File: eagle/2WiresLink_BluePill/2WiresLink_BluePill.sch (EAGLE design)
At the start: 55 parts, among them IC1 TPS54060DGQ, IC3 SN74LVC1G240DBVR, IC6 TS3021ILT

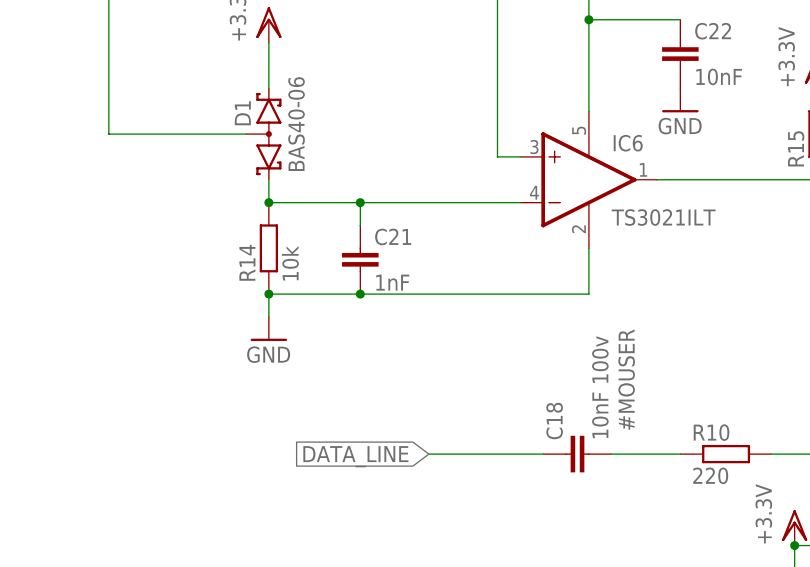
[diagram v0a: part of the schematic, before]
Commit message: eagle: increase C21 capacity from 1nF to 10nF
In previous commit carry frequency and baud rate was decreased,
C21 capacity should be increased.
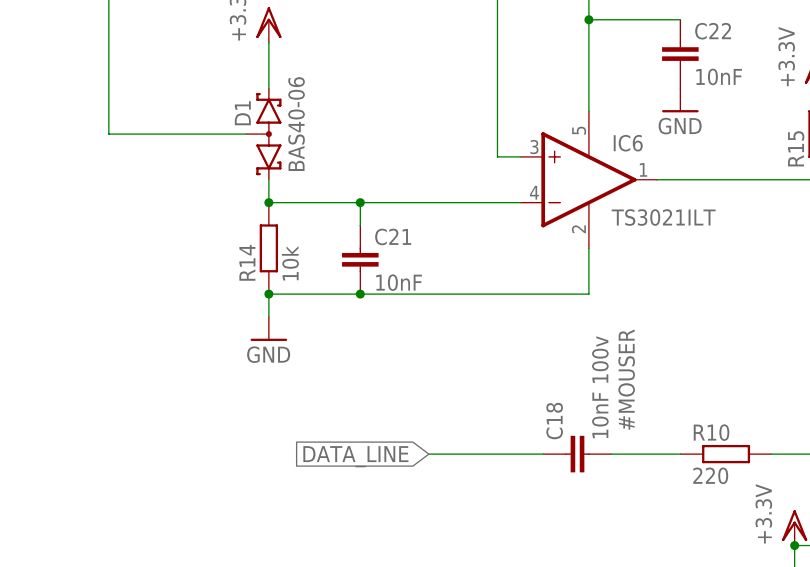
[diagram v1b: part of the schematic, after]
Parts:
- C21: value 1nF -> 10nF; MPN C0603C101J5GACTU -> (none); OC_MOUSER 80-C0603C101J5G -> (none)
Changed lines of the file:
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@@
 <attribute name="OC_NEWARK" value="unknown"/>
 </part>
-<part name="C21" library="rcl" library_urn="urn:adsk.eagle:library:334" deviceset="C-EU" device="C0603" package3d_urn="urn:adsk.eagle:package:23616/2" value="1nF">
+<part name="C21" library="rcl" library_urn="urn:adsk.eagle:library:334" deviceset="C-EU" device="C0603" package3d_urn="urn:adsk.eagle:package:23616/2" value="10nF">
 <spice>
 <pinmapping spiceprefix="C">
@@
 </spice>
 <attribute name="MF" value="KEMET"/>
-<attribute name="MPN" value="C0603C101J5GACTU"/>
-<attribute name="OC_FARNELL" value="unknown"/>
-<attribute name="OC_MOUSER" value="80-C0603C101J5G"/>
+<attribute name="OC_FARNELL" value="unknown"/>
 <attribute name="OC_NEWARK" value="unknown"/>
 </part>
@@
 <attribute name="OC_NEWARK" x="-33.02" y="5.08" size="1.778" layer="96" display="off"/>
 <attribute name="MF" x="-33.02" y="5.08" size="1.778" layer="96" display="off"/>
-<attribute name="MPN" x="-33.02" y="5.08" size="1.778" layer="96" display="off"/>
 <attribute name="OC_FARNELL" x="-33.02" y="5.08" size="1.778" layer="96" display="off"/>
-<attribute name="OC_MOUSER" x="-33.02" y="5.08" size="1.778" layer="96" display="off"/>
 </instance>
 <instance part="GND17" gate="1" x="-43.18" y="-5.08" smashed="yes">
